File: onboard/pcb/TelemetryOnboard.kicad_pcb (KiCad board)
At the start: 4 copper layers, 95 x 95 mm, 146 parts, among them J1 USB-C, J2 USB-C, J3 RFPC-SMA28-F, J4 RFPC-SMA28-F, M1 M4 Mounting Hole, M2 M4 Mounting Hole, M3 M4 Mounting Hole, M4 M4 Mounting Hole, Q1 NPN, U1 CP2102N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

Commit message: add connector to umbilical connector
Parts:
- added D29: red, LED_SMD:LED_0805_2012Metric_Pad1.15x1.40mm_HandSolder, F.Cu at (-30.0, -74.0)
- added D30: red, LED_SMD:LED_0805_2012Metric_Pad1.15x1.40mm_HandSolder, F.Cu at (-30.0, -77.0)
- added J5: Molex_MicroFit_2pin, Footprints:Molex_MicroFit_2pin, F.Cu at (-23.0, -35.5)
- added R22: 1k, Resistor_SMD:R_0805_2012Metric_Pad1.20x1.40mm_HandSolder, F.Cu at (-30.0, -80.0)
- added R51: 1k, Resistor_SMD:R_0805_2012Metric_Pad1.20x1.40mm_HandSolder, F.Cu at (-30.0, -83.0)
- moved R36 61.6 mm to (-56.2, -75.9)
- moved R23 61.6 mm to (-70.0, -75.5)
- moved R26 61.6 mm to (-70.0, -81.5)
- moved R32 61.6 mm to (-61.0, -70.0)
- moved R33 61.6 mm to (-56.0, -68.0)
- moved R35 61.6 mm to (-56.2, -78.8)
- moved R37 61.6 mm to (-56.2, -73.0)
- moved R38 61.6 mm to (-60.5, -81.5)
- moved R39 61.6 mm to (-60.5, -78.5)
- moved R40 61.6 mm to (-60.5, -75.6)
- moved R41 61.6 mm to (-68.0, -71.5)
- moved R34 16.5 mm to (-11.0, -5.00)
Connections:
- U5 pad 58: unconnected-(U5-PG4-Pad58) -> TX5
- U5 pad 59: unconnected-(U5-PG5-Pad59) -> RX5

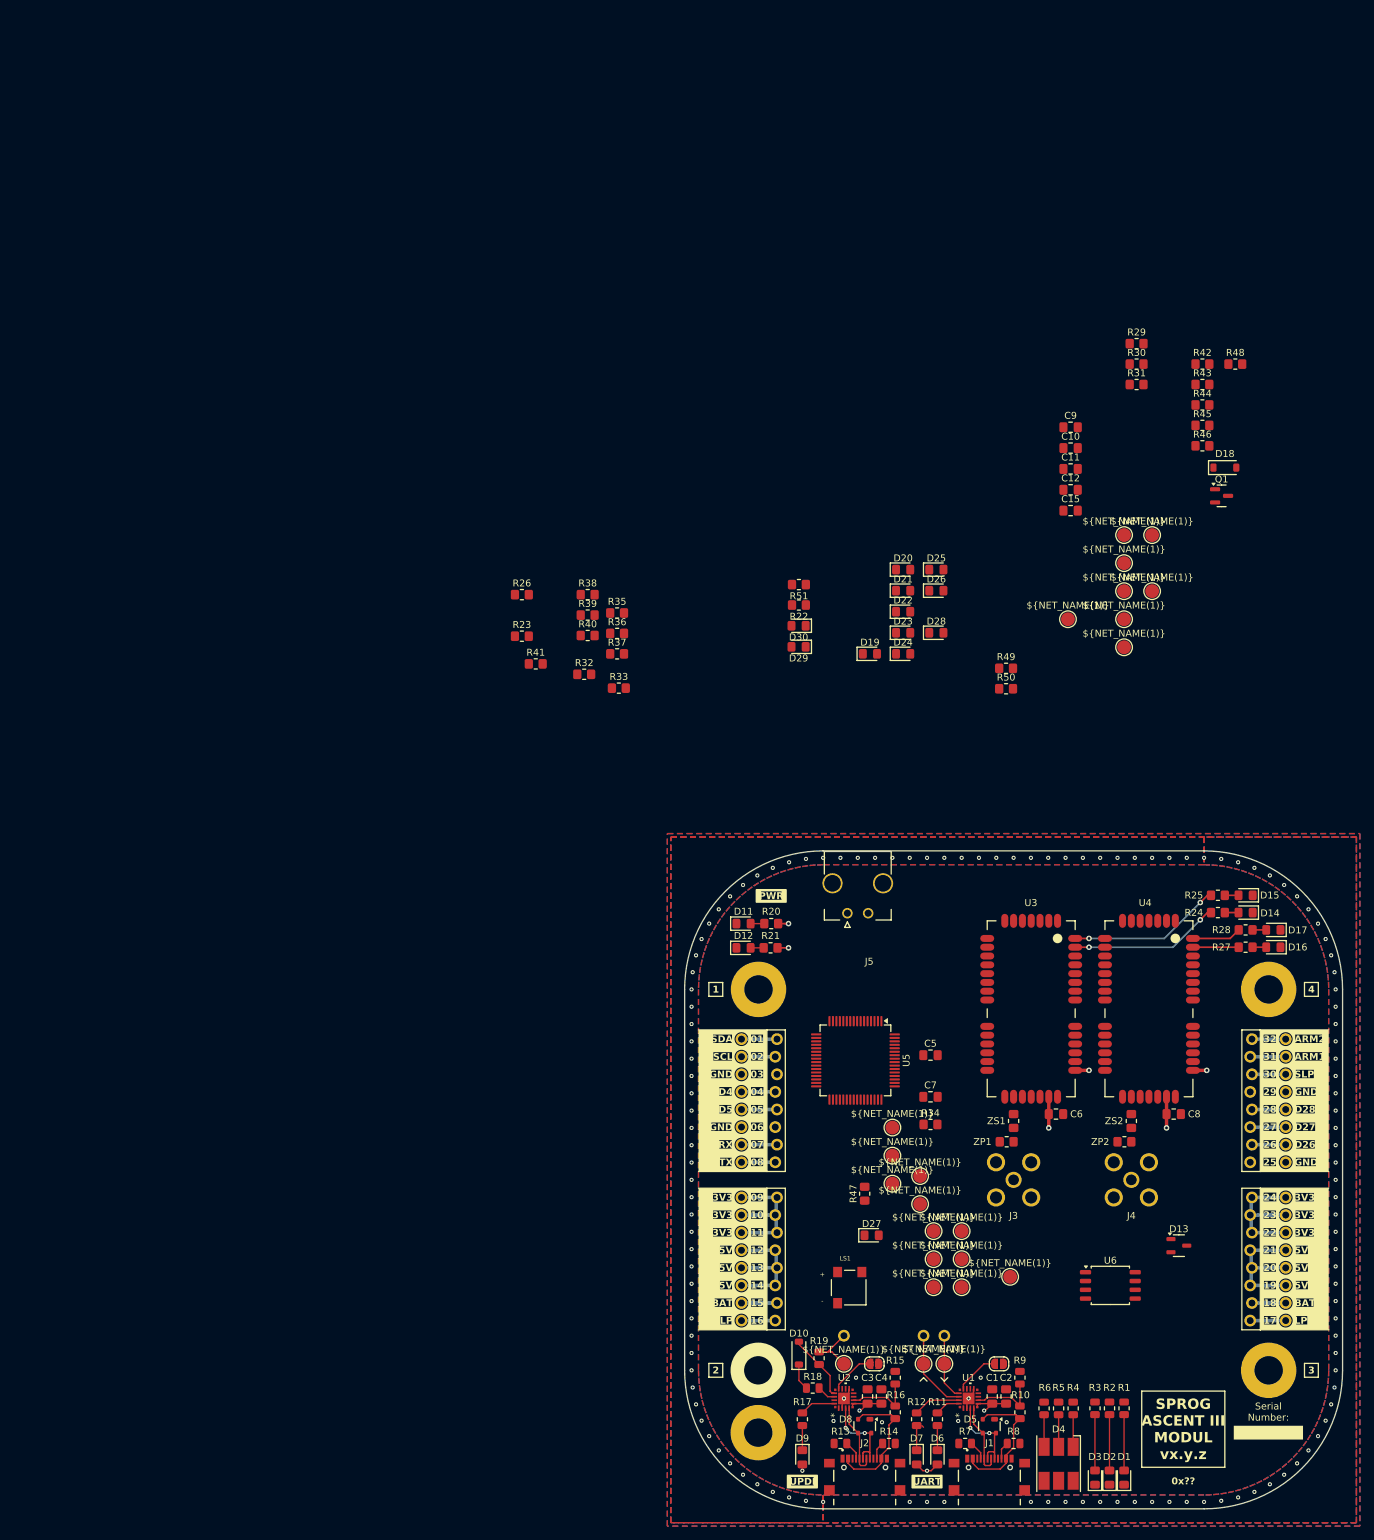
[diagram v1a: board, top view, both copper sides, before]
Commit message: place some components
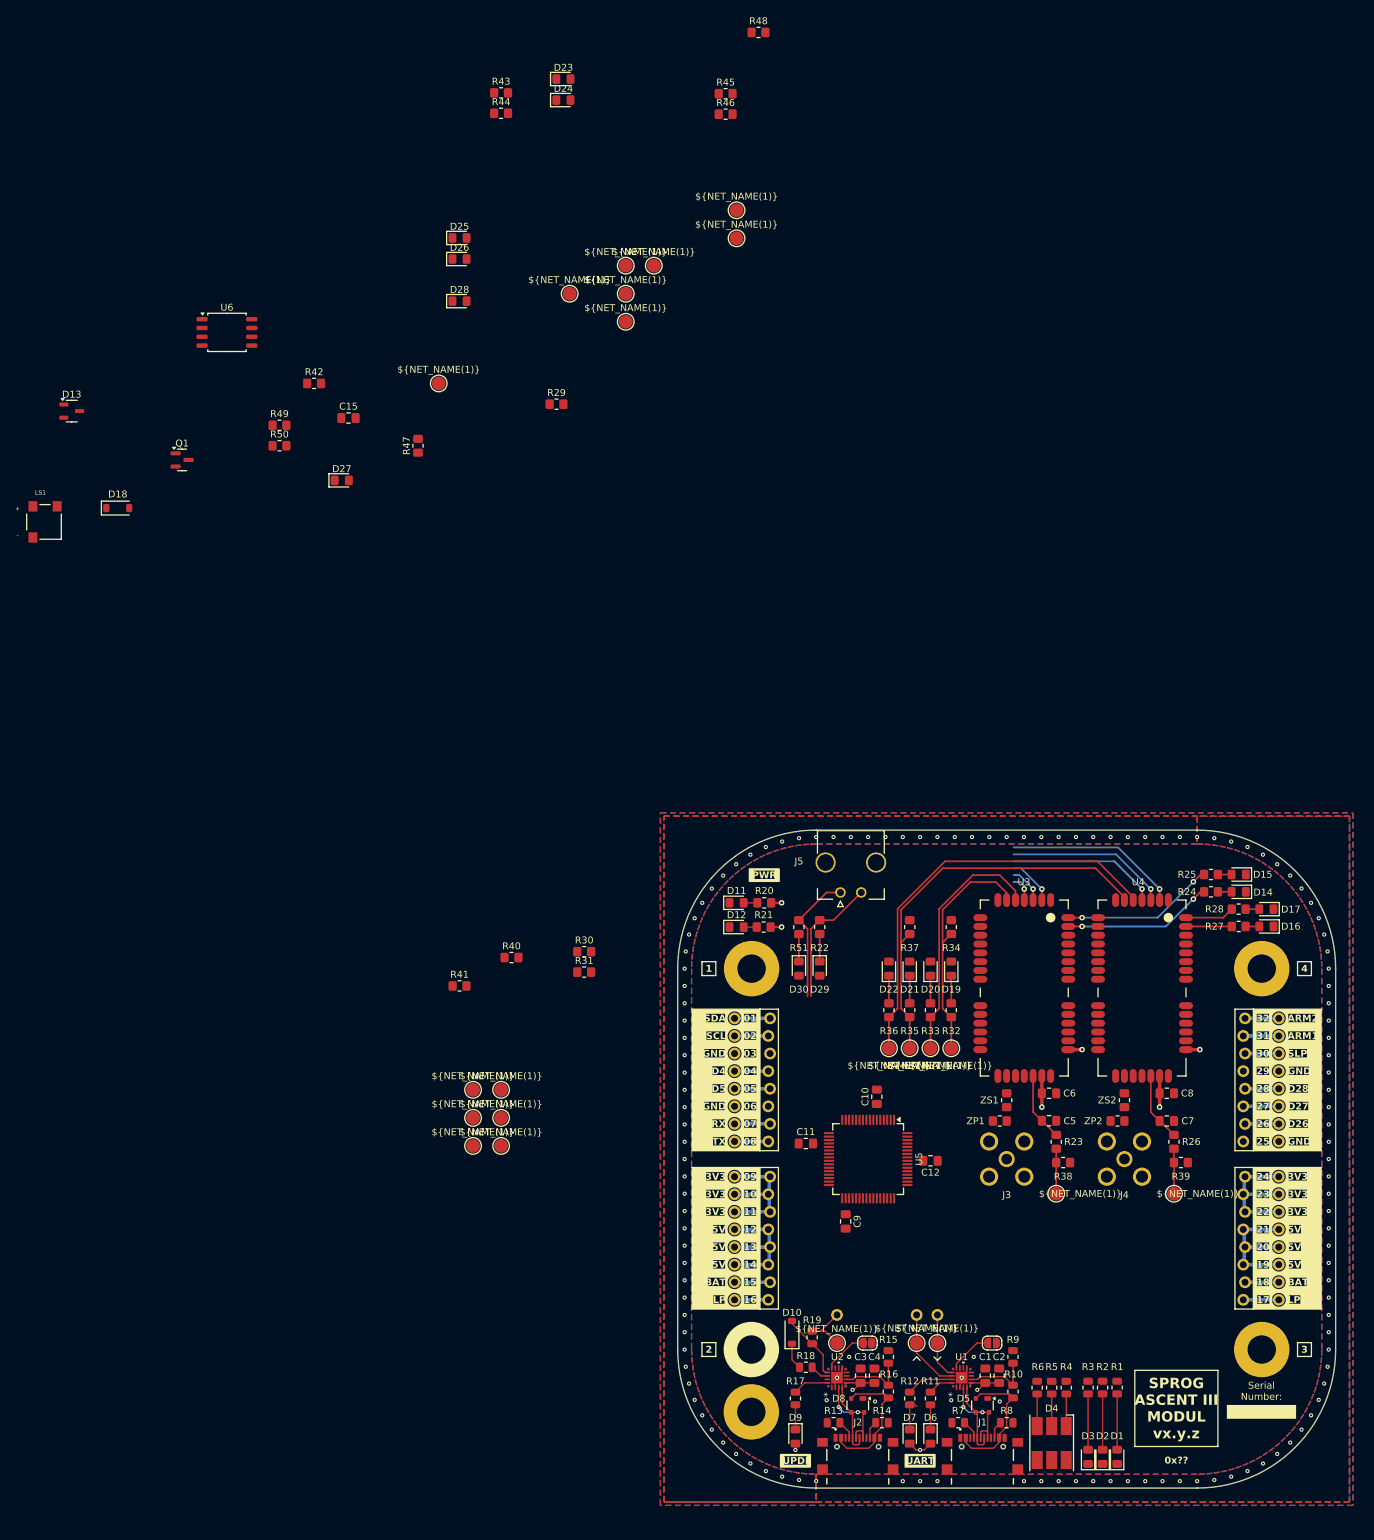
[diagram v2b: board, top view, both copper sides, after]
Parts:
- moved D13 200.2 mm to (-135.0, -108.0)
- moved U6 187.6 mm to (-112.6, -119.4)
- moved LS1 160.4 mm to (-139.0, -92.0)
- moved D18 160.0 mm to (-128.3, -94.0)
- moved Q1 150.2 mm to (-119.1, -101.0)
- moved D27 133.2 mm to (-96.0, -98.0)
- moved R42 128.3 mm to (-100.0, -112.0)
- moved R47 125.8 mm to (-85.0, -103.0)
- moved R26 122.9 mm to (24.2, -2.50), turned to -90 degrees
- moved C9 119.2 mm to (-23.2, 9.00), turned to -90 degrees
- moved R39 116.6 mm to (25.2, 0.50)
- moved R30 116.4 mm to (-61.0, -29.9)
- moved R31 116.4 mm to (-61.0, -27.0)
- moved R49 110.6 mm to (-105.0, -106.0)
- moved R50 110.6 mm to (-105.0, -103.0)
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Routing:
- net RX1: track 0.00 -> 60.1 mm
- net TX1: track 0.00 -> 59.2 mm
- net RX0: track 0.00 -> 36.0 mm
- net TX0: track 0.00 -> 34.9 mm
- net CTS2: track 0.00 -> 25.2 mm, vias 0 -> 1
- net RTS2: track 0.00 -> 23.5 mm, vias 0 -> 1
- net CFG2: track 0.00 -> 21.8 mm, vias 0 -> 1
- net TX5: track 0.00 -> 19.2 mm
- net RX5: track 0.00 -> 19.2 mm
- net Net-(U4-RESET): track 0.00 -> 9.93 mm
- net Net-(U3-RESET): track 0.00 -> 9.91 mm
- net CTS1: track 0.00 -> 6.92 mm, vias 0 -> 1
- net RST2: track 0.00 -> 6.50 mm
- net RST1: track 0.00 -> 6.50 mm
- net RTS1: track 0.00 -> 5.24 mm, vias 0 -> 1
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
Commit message: place other components on pcb
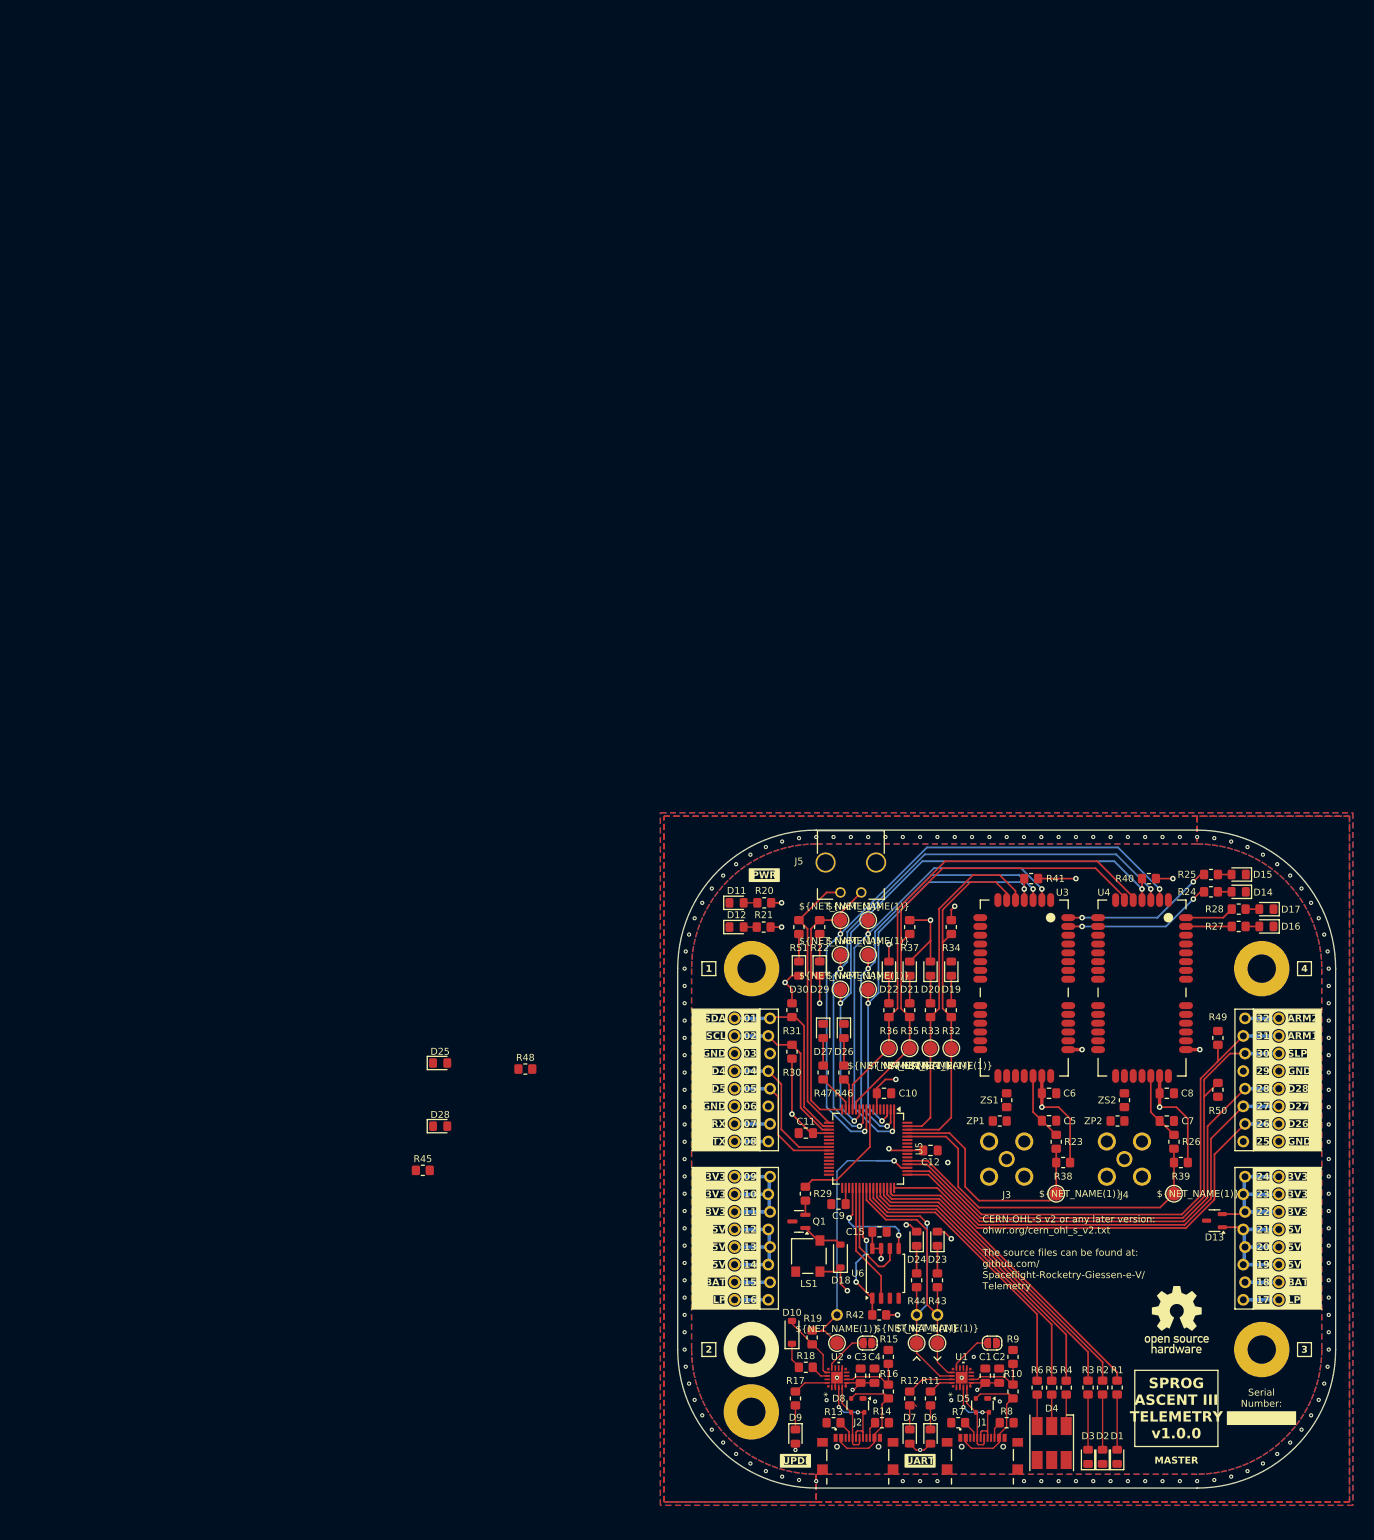
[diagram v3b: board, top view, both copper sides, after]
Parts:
- removed TP18, TP19, TP36, TP37, TP38, TP39, TP41, TP9: TestPoint, Footprints:Test Point
- R1, R10, R11, R12, R13, R14, R15, R16, R17, R18, R19, R2, R3, R4, R5, R6, R7, R8, R9: footprint Resistor_SMD:R_0805_2012Metric -> Resistor_SMD:R_0805_2012Metric_Pad1.20x1.40mm_HandSolder
- moved D13 202.2 mm to (30.0, 8.89), turned to 180 degrees
- moved R43 182.7 mm to (-10.0, 17.5), turned to -90 degrees
- moved R44 178.9 mm to (-13.0, 17.5), turned to 90 degrees
- moved D23 175.9 mm to (-10.0, 11.5), turned to 90 degrees
- moved D24 172.1 mm to (-13.0, 11.5), turned to 90 degrees
- moved U6 165.8 mm to (-17.5, 16.5), turned to 90 degrees
- moved R50 164.3 mm to (30.5, -10.0), turned to -90 degrees
- moved R49 161.8 mm to (30.5, -17.5), turned to 90 degrees
- moved R45 161.5 mm to (-84.3, 1.62)
- moved R42 157.3 mm to (-18.4, 22.5)
- moved R48 153.4 mm to (-69.5, -13.0)
- moved LS1 153.1 mm to (-28.6, 14.0), turned to 180 degrees
- moved D18 150.2 mm to (-24.0, 14.0), turned to 90 degrees
- moved Q1 141.5 mm to (-30.0, 9.00), turned to 180 degrees
- moved C15 140.3 mm to (-18.4, 10.5), turned to 180 degrees
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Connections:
- J5 pad 1: TX5 -> RX1
- J5 pad 2: RX5 -> TX1
- R22 pad 1: RX5 -> Net-(D29-K)
- R22 pad 2: Net-(D29-K) -> TX1
- R35 pad 2: TX1 -> TX3
- R36 pad 1: RX1 -> RX3
- R37 pad 1: TX1 -> TX3
- R46 pad 2: Net-(U5-PD2) -> Net-(U5-PB6)
- R47 pad 2: Net-(U5-PD0) -> Net-(U5-PB7)
- R51 pad 1: Net-(D30-K) -> RX1
- R51 pad 2: TX5 -> Net-(D30-K)
- REF** pad 1: TX -> TX4
- REF** pad 1: RX -> RX4
- TP13 pad 1: RTS2 -> CTS2
- TP14 pad 1: CTS2 -> RTS2
- TP16 pad 1: TX1 -> TX3
- TP17 pad 1: RX1 -> RX3
- TP4 pad 1: CTS1 -> RTS1
- TP8 pad 1: RTS1 -> CTS1
- U4 pad 5: RX1 -> RX3
- U4 pad 6: TX1 -> TX3
- U5 pad 1: RST1 -> CTS1
- U5 pad 10: unconnected-(U5-PB2-Pad10) -> RTS2
- U5 pad 11: unconnected-(U5-PB3-Pad11) -> CFG2
- U5 pad 12: RST2 -> TX3
- U5 pad 13: RTS2 -> RX3
- U5 pad 14: CTS2 -> Net-(U5-PB6)
- U5 pad 15: CFG2 -> Net-(U5-PB7)
- U5 pad 2: TX0 -> RTS1
- U5 pad 22: D4 -> unconnected-(U5-PC4-Pad22)
- U5 pad 23: D5 -> unconnected-(U5-PC5-Pad23)
- U5 pad 24: unconnected-(U5-PC6-Pad24) -> D4
- U5 pad 25: unconnected-(U5-PC7-Pad25) -> D5
- U5 pad 26: Net-(U5-PD0) -> unconnected-(U5-PD0-Pad26)
- U5 pad 28: Net-(U5-PD2) -> unconnected-(U5-PD2-Pad28)
- U5 pad 3: RX0 -> CFG1
- U5 pad 4: CTS1 -> unconnected-(U5-PA6-Pad4)
- U5 pad 45: LED 1 -> LED 3
- U5 pad 47: LED 3 -> LED 1
- U5 pad 5: CFG1 -> unconnected-(U5-PA7-Pad5)
- U5 pad 58: TX5 -> unconnected-(U5-PG4-Pad58)
- U5 pad 59: RX5 -> unconnected-(U5-PG5-Pad59)
- U5 pad 60: unconnected-(U5-PG6-Pad60) -> RST2
- U5 pad 61: unconnected-(U5-PG7-Pad61) -> RST1
- U5 pad 62: unconnected-(U5-XTALHF1/PA0-Pad62) -> TX0
- U5 pad 63: unconnected-(U5-XTALHF2/PA1-Pad63) -> RX0
- U5 pad 8: RTS1 -> BUZZ
- U5 pad 9: BUZZ -> CTS2
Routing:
- net +5V: track 41.7 -> 199.7 mm
- net +3V3: track 67.6 -> 175.1 mm, vias 8 -> 23
- net ARM1: track 5.13 -> 79.8 mm
- net SLP: track 4.87 -> 79.4 mm
- net TX3: track 0.00 -> 71.6 mm
- net RX3: track 0.00 -> 71.1 mm
- net CTS2: track 25.2 -> 93.4 mm, vias 1 -> 3
- net D28: track 4.87 -> 70.6 mm
- net RTS2: track 23.5 -> 87.8 mm, vias 1 -> 3
- net D27: track 5.13 -> 68.8 mm
- net D26: track 4.87 -> 68.0 mm
- net CTS1: track 6.92 -> 70.0 mm, vias 1 -> 3
- net CFG2: track 21.8 -> 83.7 mm, vias 1 -> 3
- net RTS1: track 5.24 -> 64.3 mm, vias 1 -> 3
- net CFG1: track 3.82 -> 60.5 mm, vias 1 -> 3
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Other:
- board text added: "CERN-OHL-S v2 or any later version: ohwr.org/cern_ohl_s_v2.txt The source files can be found at: github.com/ Spaceflight-Rocketry-Giessen-e-V/ Telemetry"
- board text added: "MASTER"
- board text added: "SPROG ASCENT III TELEMETRY v1.0.0"
- board text removed: "0x??"
- board text removed: "SPROG ASCENT III MODUL vx.y.z"
